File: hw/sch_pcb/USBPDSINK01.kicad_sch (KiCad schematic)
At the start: 30 parts, among them J1 USBC_USB4105-GF-A, J2 HEADER_2x05_PARALLEL, J3 HEADER_2x04_PARALLEL, J4 HEADER_2x03_PARALLEL, Q2 PMOS, U1 STUSB4500QTR

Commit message: Navrh schema
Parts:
- removed C3: C_Small, symbol Device:C_Small
- removed JP2: Jumper_2_Open, symbol Jumper:Jumper_2_Open
- added C5, C6: 10u, Capacitor_SMD:C_0805_2012Metric, symbol Device:C_Small
- added C7, C8: 1u, Capacitor_SMD:C_0805_2012Metric, symbol Device:C_Small
- added J5: HEADER_2x01, Connector_PinHeader_2.54mm:PinHeader_2x01_P2.54mm_Vertical, symbol MLAB_HEADER:HEADER_2x01
- added J6: HEADER_2x07_PARALLEL, Connector_PinHeader_2.54mm:PinHeader_2x07_P2.54mm_Vertical, symbol MLAB_HEADER:HEADER_2x07_PARALLEL
- added JP4: Jumper_2_Open, Connector_PinHeader_2.54mm:PinHeader_2x01_P2.54mm_Vertical, symbol Jumper:Jumper_2_Open
- added M1, M2, M3, M4: HOLE, Mlab_Mechanical:MountingHole_3mm, symbol MLAB_MECHANICAL:HOLE
- added R13, R14, R15, R16, R17, R18, R19, R20, R21: R, Resistor_SMD:R_0805_2012Metric, symbol Device:R_Small
- added R22, R23: 100K, Resistor_SMD:R_0805_2012Metric, symbol Device:R_Small
- added U2: NCP1117-3.3, Package_TO_SOT_SMD:SOT-223-3_TabPin2, symbol Regulator_Linear:NCP1117-3.3_SOT223
- C1, C2, C4: footprint (none) -> Capacitor_SMD:C_0805_2012Metric
- D1, D2, D3, D4, D5: footprint (none) -> Mlab_D:LED_1206_2
- J2: footprint (none) -> Connector_PinHeader_2.54mm:PinHeader_2x05_P2.54mm_Vertical
- J3: footprint (none) -> Connector_PinHeader_2.54mm:PinHeader_2x04_P2.54mm_Vertical
- J4: footprint (none) -> Connector_PinHeader_2.54mm:PinHeader_2x03_P2.54mm_Vertical
- JP1: footprint (none) -> Connector_PinHeader_2.54mm:PinHeader_2x01_P2.54mm_Vertical
- JP3: footprint (none) -> Connector_PinHeader_2.54mm:PinHeader_1x03_P2.54mm_Vertical
- Q2: value PMOS -> IRF7469PbF; footprint (none) -> Package_SO:SOIC-8_3.9x4.9mm_P1.27mm; symbol Simulation_SPICE:PMOS -> MLAB_T:IRF7469PbF
- R1, R10, R11, R12, R2, R3, R4, R5, R6, R7, R8, R9: footprint (none) -> Resistor_SMD:R_0805_2012Metric
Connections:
- net VDD is gone; now on net GND: J2.5, J2.6
- net ADDR1: now also R23.1
- net ALERT: now also D1.1 (K), J6.1, J6.2, R15.2; no longer R6.1
- net ATTACH: now also D5.1 (K), J6.5, J6.6, R17.2; no longer R7.1
- net GND: now also J4.3, J4.4, C5.2, C6.2, C7.2, C8.2, M1.1, M2.1, M3.1, M4.1, R22.1, R23.2, U2.1 (GND); no longer D1.1 (K), D2.1 (K), D3.1 (K), D4.1 (K), D5.1 (K)
- net GPIO: now also D2.1 (K), J6.7, J6.8, R18.2; no longer R5.1
- net PWR_OK2: now also D3.1 (K), J6.10, J6.9, R19.2; no longer R4.1
- net PWR_OK3: now also D4.1 (K), J6.11, J6.12, R20.2; no longer R3.1
- net RESET: now also J6.13, J6.14, R21.2
- net SCL: now also R14.2
- net SDA: now also R13.2
- net SIDE: now also J6.3, J6.4, R16.2
- net VBUS: now also Q2.1 (S), Q2.2 (S), C6.1, C8.1, U2.3 (VI)
- net VCC: now also JP3.2 (C), JP4.2 (B), R13.1, R14.1, R15.1, R16.1, R17.1, R18.1, R19.1, R20.1, R21.1; no longer J4.3, J4.4, JP3.1 (A)
- net VOUT: now also Q2.5 (D), Q2.6 (D), Q2.7 (D), Q2.8 (D); no longer Q2.1 (D)
- net VSYS: now also C7.1, JP4.1 (A), R22.2; no longer JP3.2 (C)
- net at R10.2, R11.2, R12.1: now also Q2.4 (G); no longer Q2.2 (G)
- net at J1.A6 (D+): now also J1.B6 (D+), J5.1
- net at J1.A7 (D-): now also J1.B7 (D-), J5.2
- new net +3V3: C5.1, JP3.1 (A), R3.1, R4.1, R5.1, R6.1, R7.1, U2.2 (VO)
- no-connect marks 0 -> 2
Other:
- note added: "+ WAGO???"
- note added: "Secondary power enable"
- moved on the sheet: J2, J3, J4

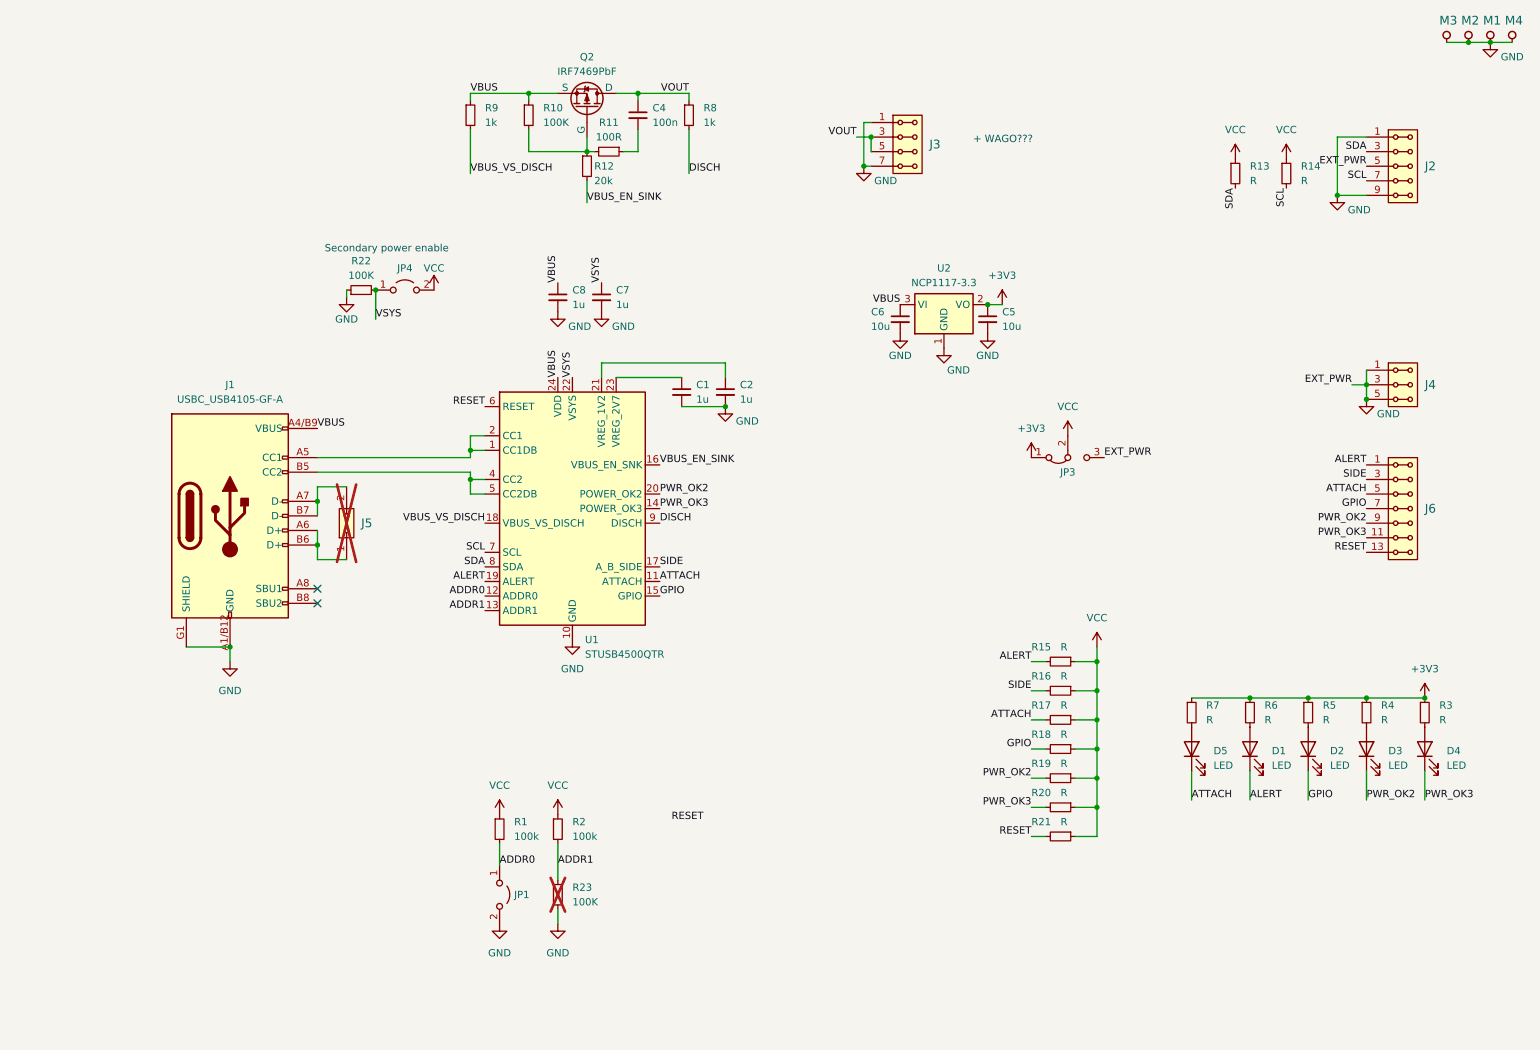
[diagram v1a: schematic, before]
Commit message: update improvements in schematics and layout
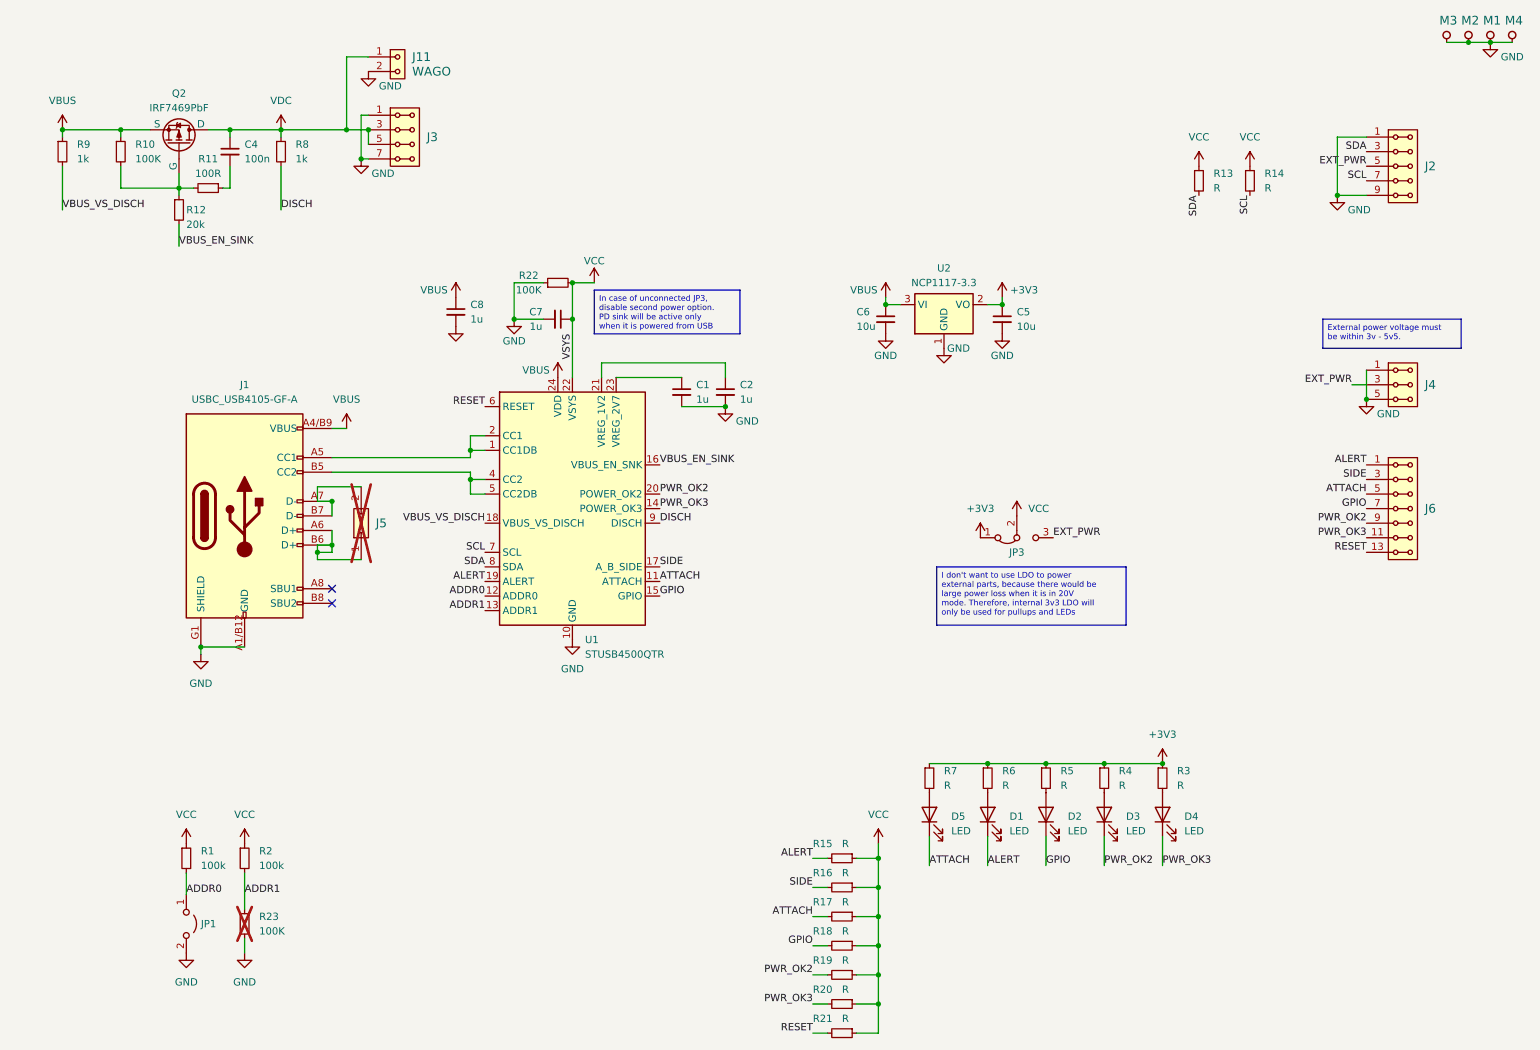
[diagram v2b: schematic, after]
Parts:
- removed JP4: Jumper_2_Open, Connector_PinHeader_2.54mm:PinHeader_2x01_P2.54mm_Vertical, symbol Jumper:Jumper_2_Open
- added J11: WAGO, TerminalBlock_WAGO:TerminalBlock_WAGO_236-102_1x02_P5.00mm_45Degree, symbol MLAB_HEADER:HEADER_1x02
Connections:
- net VSYS is gone; now on net VCC: C7.1, R22.2, U1.22 (VSYS)
- net GND: now also J11.2; no longer J2.5, J2.6, J4.3, J4.4, JP3.3 (B)
- net VOUT renamed VDC
- net VDC: now also J11.1
- new net EXT_PWR: J2.5, J2.6, J4.3, J4.4, JP3.3 (B)
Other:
- note removed: "+ WAGO???"
- note removed: "Secondary power enable"
- moved on the sheet: C4, C5, C6, C7, C8, D1, D2, D3, D4, D5, J1, J3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

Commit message: update component values
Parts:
- D1, D4: value LED -> RED
- D2: value LED -> YELLOW
- D3: value LED -> ORANGE
- D5: value LED -> GREEN
- J11: value WAGO -> WAGO_236-102_1x02
- R13, R14, R15, R16, R17, R18, R19, R20, R21: value R -> 4k7
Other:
- moved on the sheet: D1, D2, D3, D4, R3, R4, R5, R6

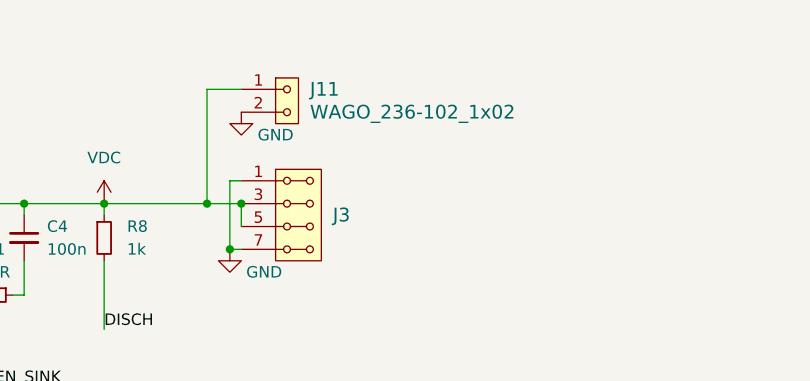
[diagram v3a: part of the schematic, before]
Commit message: update wago connector
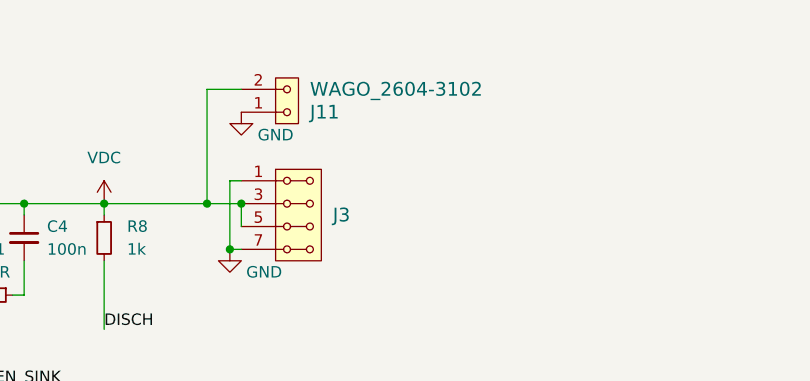
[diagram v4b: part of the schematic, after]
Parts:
- J11: value WAGO_236-102_1x02 -> WAGO_2604-3102; footprint TerminalBlock_WAGO:TerminalBlock_WAGO_236-102_1x02_P5.00mm_45Degree -> Mlab_CON:TerminalBlock_WAGO_2604-3102_1x02_P5.00mm_Vertical
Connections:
- net GND: now also J11.1; no longer J11.2
- net VDC: now also J11.2; no longer J11.1
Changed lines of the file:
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@@
     )
   )
-  (symbol (lib_id "MLAB_HEADER:HEADER_1x02") (at 85.09 22.86 0) (unit 1)
+  (symbol (lib_id "MLAB_HEADER:HEADER_1x02") (at 85.09 22.86 0) (mirror x) (unit 1)
     (in_bom yes) (on_board yes) (dnp no)
-    (property "Reference" "J11" (at 87.63 21.59 0)
+    (property "Reference" "J11" (at 87.63 24.13 0)
       (effects (font (size 1.524 1.524)) (justify left))
     )
-    (property "Value" "WAGO_236-102_1x02" (at 87.63 24.13 0)
+    (property "Value" "WAGO_2604-3102" (at 87.63 21.59 0)
       (effects (font (size 1.524 1.524)) (justify left))
     )
-    (property "Footprint" "TerminalBlock_WAGO:TerminalBlock_WAGO_236-102_1x02_P5.00mm_45Degree" (at 85.09 21.59 0)
+    (property "Footprint" "Mlab_CON:TerminalBlock_WAGO_2604-3102_1x02_P5.00mm_Vertical" (at 85.09 24.13 0)
       (effects (font (size 1.524 1.524)) hide)
     )
-    (property "Datasheet" "" (at 85.09 21.59 0)
+    (property "Datasheet" "" (at 85.09 24.13 0)
       (effects (font (size 1.524 1.524)))
     )

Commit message: set sheet template
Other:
- company: (none) -> www.mlab.cz
- title: (none) -> USBPDSINK01A
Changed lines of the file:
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@@
 (kicad_sch (version 20230121) (generator eeschema)
   (paper "A4")
+  (title_block
+    (title "USBPDSINK01A")
+    (company "www.mlab.cz")
+    (comment 1 "USB-C PD sink controller")
+    (comment 2 "roman-dvorak <romandvorak@mlab.cz>")
+  )
   (junction (at 224.79 144.78) (diameter 0) (color 0 0 0 0)
   )
